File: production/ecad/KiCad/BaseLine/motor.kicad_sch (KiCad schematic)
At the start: 2 parts, among them M1 Motor_DC, U2 DRV8830DGQR

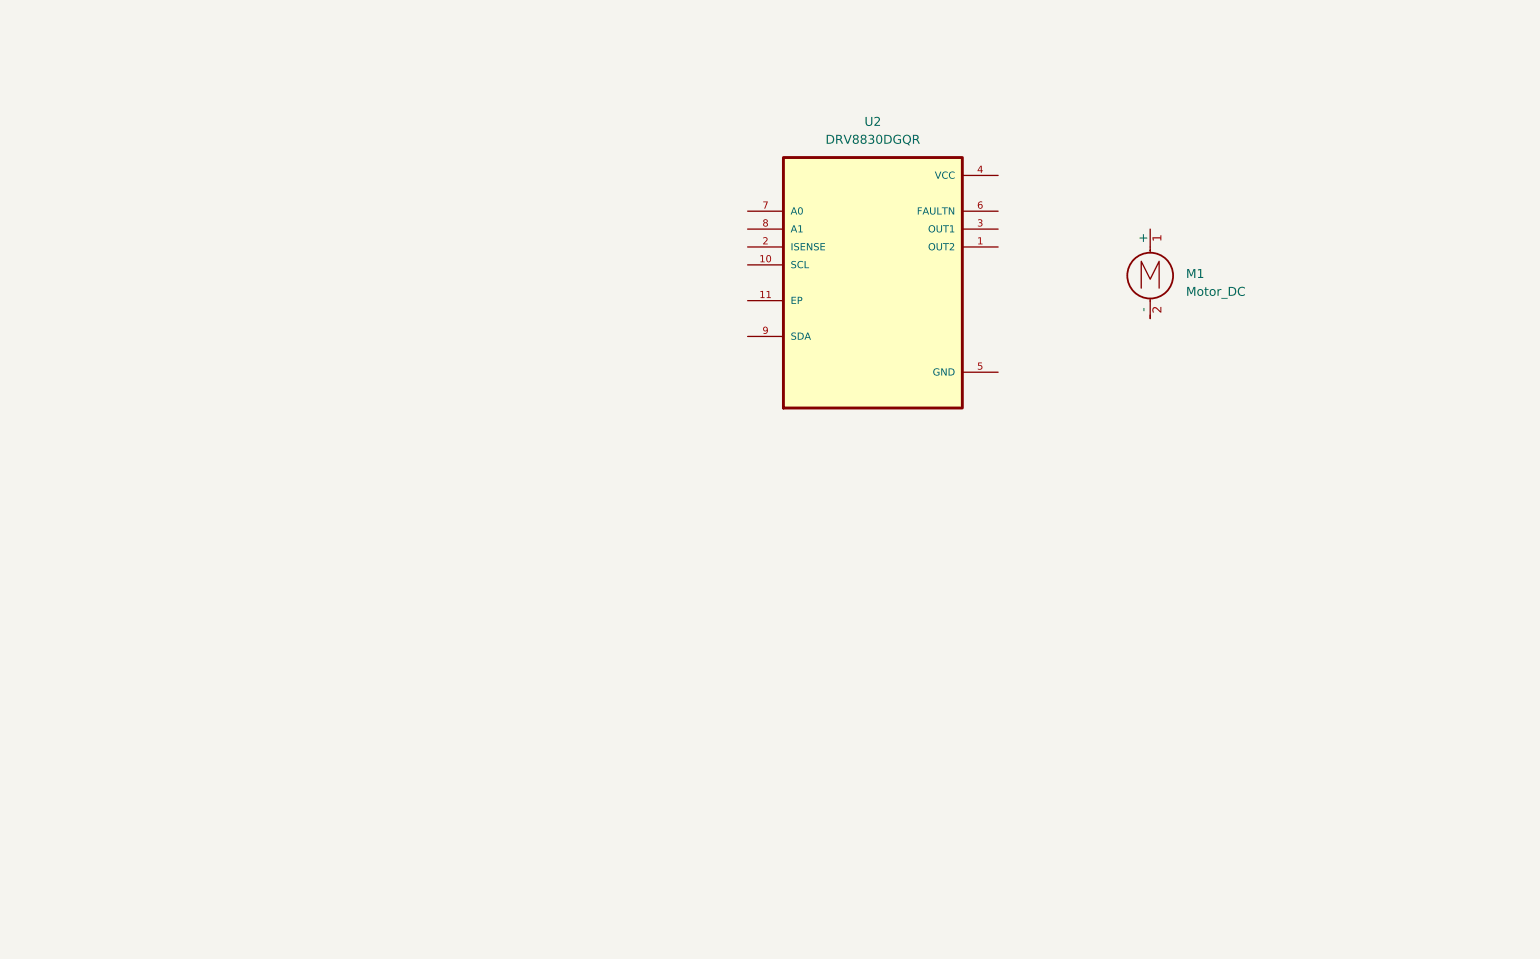
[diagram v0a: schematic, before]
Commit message: Added schematic for vibe motor
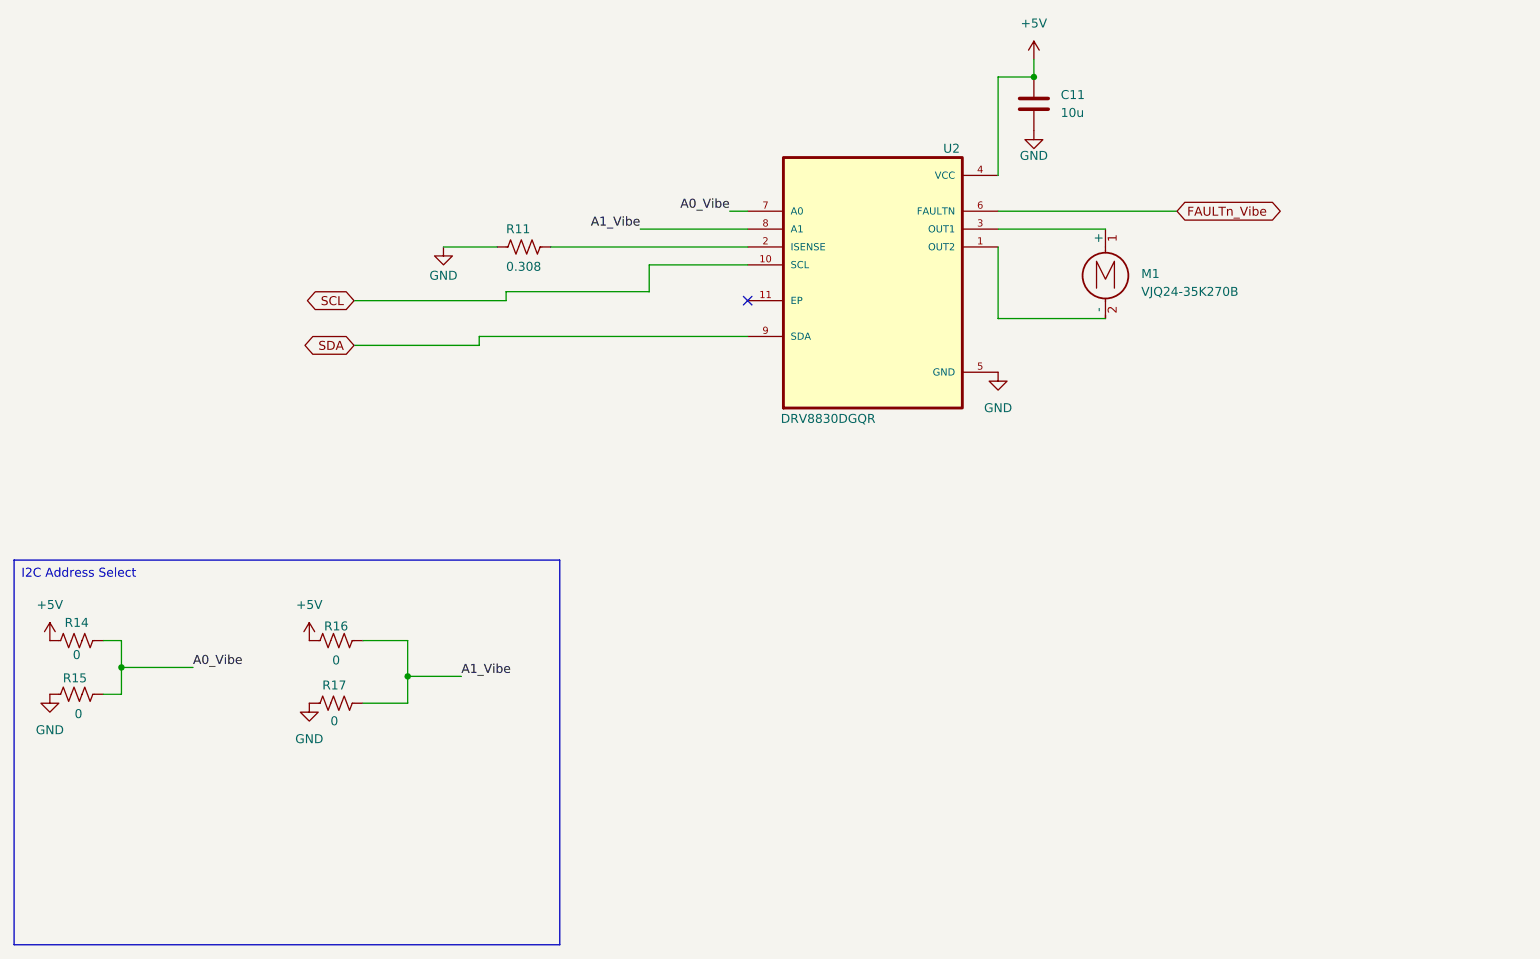
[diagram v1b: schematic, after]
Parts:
- added C11: 10u, symbol Device:C
- added R11: 0.308, symbol Device:R_US
- added R14, R15, R16, R17: 0, symbol Device:R_US
- M1: value Motor_DC -> VJQ24-35K270B
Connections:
- net at U2.1 (OUT2): now also M1.2 (-)
- net SCL: now reaches U2.10 (SCL)
- net at U2.2 (ISENSE): now also R11.1
- net at U2.3 (OUT1): now also M1.1 (+)
- net +5V: now reaches U2.4 (VCC)
- net +5V: now also C11.1, R14.1, R16.1
- net GND: now reaches U2.5 (GND)
- net GND: now also C11.2, R11.2, R15.1, R17.1
- net FAULTn_Vibe: now reaches U2.6 (FAULTN)
- net A0_Vibe: now reaches U2.7 (A0)
- net A0_Vibe: now also R14.2, R15.2
- net A1_Vibe: now reaches U2.8 (A1)
- net A1_Vibe: now also R16.2, R17.2
- net SDA: now reaches U2.9 (SDA)
- no-connect marks 0 -> 1
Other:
- moved on the sheet: M1

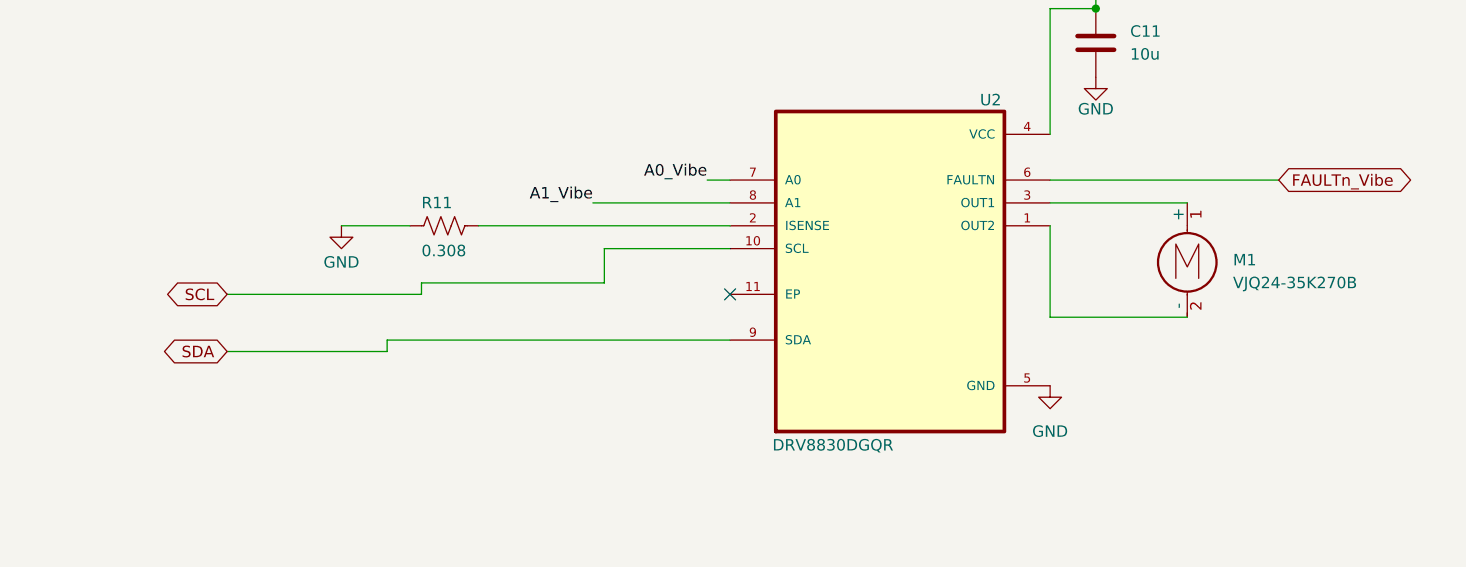
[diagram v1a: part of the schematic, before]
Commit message: Added vibe motor connector and amp I2C
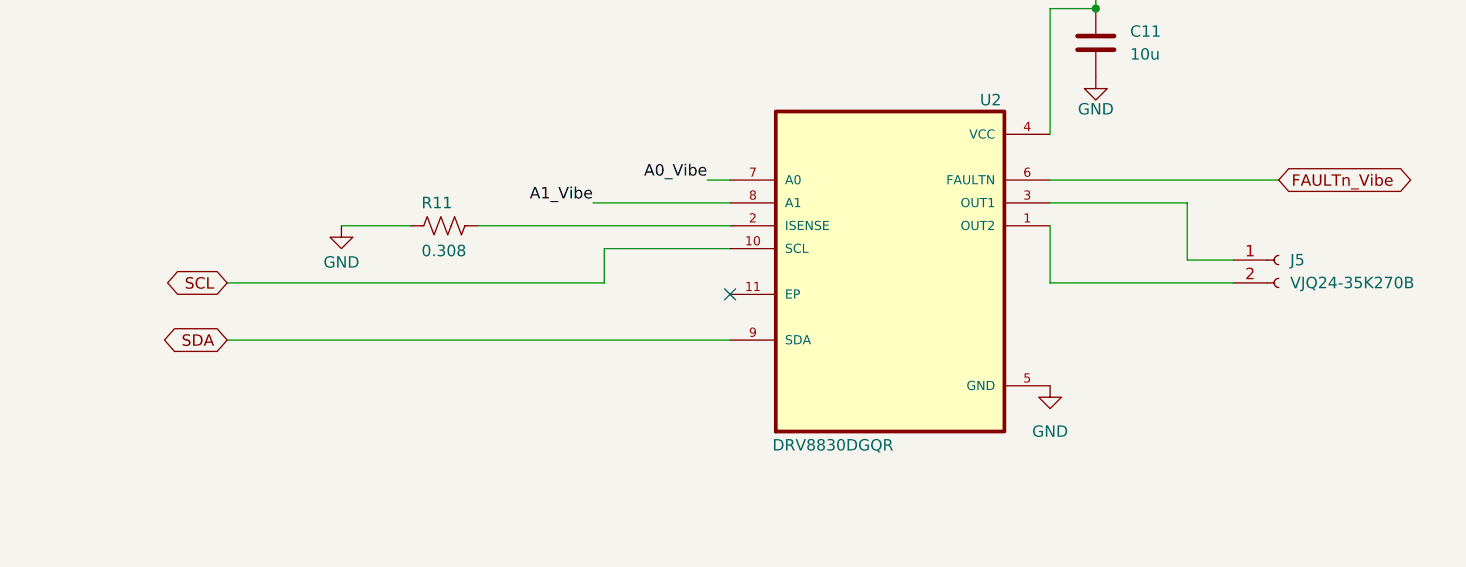
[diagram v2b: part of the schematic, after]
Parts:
- removed M1: VJQ24-35K270B, symbol Motor:Motor_DC
- added J5: VJQ24-35K270B, symbol Connector:Conn_01x02_Socket
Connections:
- net at U2.1 (OUT2): now also J5.2 (Pin_2)
- net at U2.3 (OUT1): now also J5.1 (Pin_1)
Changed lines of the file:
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@@
 	(wire
 		(pts
-			(xy 80.01 109.22) (xy 118.11 109.22)
+			(xy 168.91 100.33) (xy 173.99 100.33)
 		)
 		(stroke
@@
 	(wire
 		(pts
-			(xy 83.82 102.87) (xy 104.14 102.87)
+			(xy 153.67 102.87) (xy 153.67 96.52)
 		)
 		(stroke
@@
 	(wire
 		(pts
-			(xy 153.67 96.52) (xy 153.67 106.68)
+			(xy 29.21 152.4) (xy 26.67 152.4)
 		)
 		(stroke
@@
 	(wire
 		(pts
-			(xy 83.82 104.14) (xy 83.82 102.87)
+			(xy 153.67 72.39) (xy 153.67 86.36)
 		)
 		(stroke
@@
 	(wire
 		(pts
-			(xy 29.21 152.4) (xy 26.67 152.4)
+			(xy 168.91 93.98) (xy 168.91 100.33)
 		)
 		(stroke
@@
 	(wire
 		(pts
-			(xy 80.01 110.49) (xy 80.01 109.22)
+			(xy 153.67 72.39) (xy 158.75 72.39)
 		)
 		(stroke
@@
 	(wire
 		(pts
-			(xy 153.67 72.39) (xy 153.67 86.36)
+			(xy 90.17 96.52) (xy 118.11 96.52)
 		)
 		(stroke
@@
 	(wire
 		(pts
-			(xy 153.67 72.39) (xy 158.75 72.39)
+			(xy 104.14 99.06) (xy 118.11 99.06)
 		)
 		(stroke
@@
 	(wire
 		(pts
-			(xy 90.17 96.52) (xy 118.11 96.52)
+			(xy 63.5 152.4) (xy 69.85 152.4)
 		)
 		(stroke
@@
 	(wire
 		(pts
-			(xy 104.14 99.06) (xy 118.11 99.06)
+			(xy 62.23 102.87) (xy 104.14 102.87)
 		)
 		(stroke
@@
 	(wire
 		(pts
-			(xy 63.5 152.4) (xy 69.85 152.4)
+			(xy 115.57 91.44) (xy 118.11 91.44)
 		)
 		(stroke
@@
 	(wire
 		(pts
-			(xy 62.23 104.14) (xy 83.82 104.14)
+			(xy 29.21 160.02) (xy 29.21 156.21)
 		)
 		(stroke
@@
 	(wire
 		(pts
-			(xy 115.57 91.44) (xy 118.11 91.44)
+			(xy 153.67 91.44) (xy 179.07 91.44)
 		)
 		(stroke
@@
 	(wire
 		(pts
-			(xy 29.21 160.02) (xy 29.21 156.21)
+			(xy 39.37 156.21) (xy 29.21 156.21)
 		)
 		(stroke
@@
 	(wire
 		(pts
-			(xy 153.67 91.44) (xy 179.07 91.44)
+			(xy 62.23 109.22) (xy 118.11 109.22)
 		)
 		(stroke
@@
 	(wire
 		(pts
-			(xy 39.37 156.21) (xy 29.21 156.21)
+			(xy 69.85 157.48) (xy 77.47 157.48)
 		)
 		(stroke
@@
 	(wire
 		(pts
-			(xy 62.23 110.49) (xy 80.01 110.49)
+			(xy 69.85 157.48) (xy 69.85 161.29)
 		)
 		(stroke
@@
 	(wire
 		(pts
-			(xy 69.85 157.48) (xy 77.47 157.48)
-		)
-		(stroke
-			(width 0)
-			(type default)
-		)
-	)
-	(wire
-		(pts
-			(xy 153.67 106.68) (xy 168.91 106.68)
-		)
-		(stroke
-			(width 0)
-			(type default)
-		)
-	)
-	(wire
-		(pts
-			(xy 69.85 157.48) (xy 69.85 161.29)
+			(xy 153.67 102.87) (xy 173.99 102.87)
 		)
 		(stroke
@@
 	(global_label "SDA"
 		(shape bidirectional)
-		(at 62.23 110.49 180)
+		(at 62.23 109.22 180)
 		(fields_autoplaced yes)
 		(effects
@@
 		)
 		(property "Intersheetrefs" "${INTERSHEET_REFS}"
-			(at 54.5654 110.49 0)
+			(at 54.5654 109.22 0)
 			(effects
 				(font
@@
 	(global_label "SCL"
 		(shape bidirectional)
-		(at 62.23 104.14 180)
+		(at 62.23 102.87 180)
 		(fields_autoplaced yes)
 		(effects
@@
 		)
 		(property "Intersheetrefs" "${INTERSHEET_REFS}"
-			(at 54.6259 104.14 0)
+			(at 54.6259 102.87 0)
 			(effects
 				(font
@@
 	)
 	(symbol
+		(lib_id "Connector:Conn_01x02_Socket")
+		(at 179.07 100.33 0)
+		(unit 1)
+		(exclude_from_sim no)
+		(in_bom yes)
+		(on_board yes)
+		(dnp no)
+		(fields_autoplaced yes)
+		(property "Reference" "J5"
+			(at 180.34 100.3299 0)
+			(effects
+				(font
+					(size 1.27 1.27)
+				)
+				(justify left)
+			)
+		)
+		(property "Value" "VJQ24-35K270B"
+			(at 180.34 102.8699 0)
+			(effects
+				(font
+					(size 1.27 1.27)
+				)
+				(justify left)
+			)
+		)
+		(property "Footprint" ""
+			(at 179.07 100.33 0)
+			(effects
+				(font
+					(size 1.27 1.27)
+				)
+				(hide yes)
+			)
+		)
+		(property "Datasheet" "~"
+			(at 179.07 100.33 0)
+			(effects
+				(font
+					(size 1.27 1.27)
+				)
+				(hide yes)
+			)
+		)
+		(property "Description" "Generic connector, single row, 01x02, script generated"
+			(at 179.07 100.33 0)
+			(effects
+				(font
+					(size 1.27 1.27)
+				)
+				(hide yes)
+			)
+		)
+		(pin "2"
+		)
+		(pin "1"
+		)
+		(instances
+			(project "BaseLine"
+				(path "/ba9eda21-3882-41e1-8265-3d8ac781da20/32bcaf69-2ff4-46a9-8a42-fce7269397e2"
+					(reference "J5")
+					(unit 1)
+				)
+			)
+		)
+	)
+	(symbol
 		(lib_id "Device:C")
 		(at 158.75 76.2 0)
@@
 					(unit 1)
 				)
-			)
-		)
-	)
-	(symbol
-		(lib_id "Motor:Motor_DC")
-		(at 168.91 99.06 0)
-		(unit 1)
-		(exclude_from_sim no)
-		(in_bom yes)
-		(on_board yes)
-		(dnp no)
-		(fields_autoplaced yes)
-		(property "Reference" "M1"
-			(at 173.99 100.3299 0)
-			(effects
-				(font
-					(size 1.27 1.27)
-				)
-				(justify left)
-			)
-		)
-		(property "Value" "VJQ24-35K270B"
-			(at 173.99 102.8699 0)
-			(effects
-				(font
-					(size 1.27 1.27)
-				)
-				(justify left)
-			)
-		)
-		(property "Footprint" ""
-			(at 168.91 101.346 0)
-			(effects
-				(font
-					(size 1.27 1.27)
-				)
-				(hide yes)
-			)
-		)
-		(property "Datasheet" "https://www.digikey.com/en/products/detail/vybronics-inc/VJQ24-35K270B/7732324"
-			(at 168.91 101.346 0)
-			(effects
-				(font
-					(size 1.27 1.27)
-				)
-				(hide yes)
-			)
-		)
-		(property "Description" "DC Motor"
-			(at 168.91 99.06 0)
-			(effects
-				(font
-					(size 1.27 1.27)
-				)
-				(hide yes)
-			)
-		)
-		(pin "2"
-		)
-		(pin "1"
-		)
-		(instances
-			(project "BaseLine"
-				(path "/ba9eda21-3882-41e1-8265-3d8ac781da20/32bcaf69-2ff4-46a9-8a42-fce7269397e2"
-					(reference "M1")
-					(unit 1)
-				)

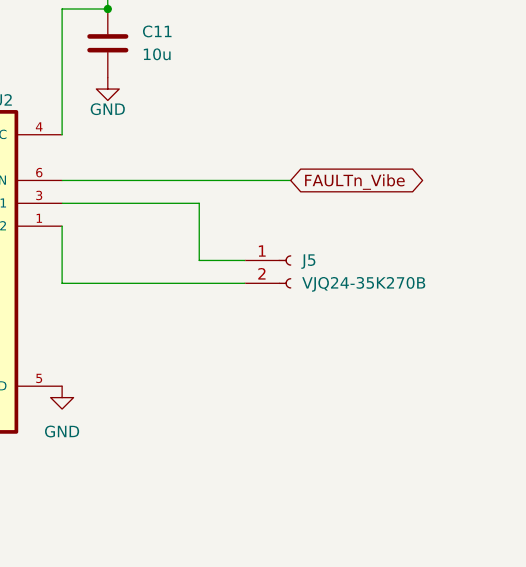
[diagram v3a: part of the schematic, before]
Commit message: Updated with new load cell amp IC
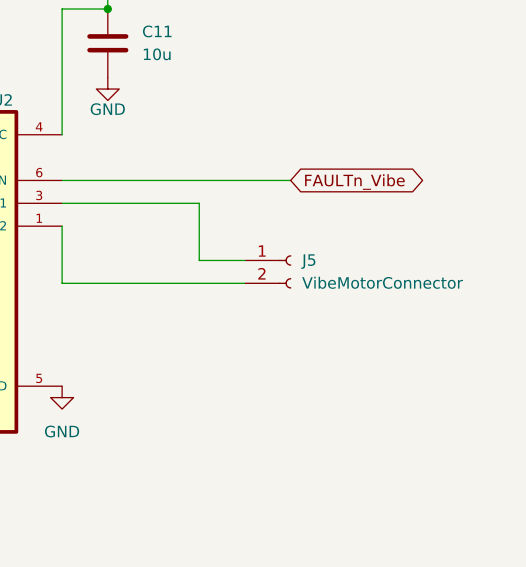
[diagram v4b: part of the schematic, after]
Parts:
- J5: value VJQ24-35K270B -> VibeMotorConnector
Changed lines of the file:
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@@
 			)
 		)
-		(property "Value" "VJQ24-35K270B"
+		(property "Value" "VibeMotorConnector"
 			(at 180.34 102.8699 0)
 			(effects
@@
 			)
 		)
-		(property "Datasheet" "~"
+		(property "Datasheet" "https://www.digikey.com/en/products/detail/vybronics-inc/VJQ24-35K270B/7732324?s=N4IgTCBcDaIGoCkCKYAsBaAzAVgNJgHYAGAIRAF0BfIA"
 			(at 179.07 100.33 0)
 			(effects
@@
 			)
 		)
-		(property "Description" "Generic connector, single row, 01x02, script generated"
+		(property "Description" "VJQ24-35K270B"
 			(at 179.07 100.33 0)
 			(effects

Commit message: Updates
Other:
- moved on the sheet: J5
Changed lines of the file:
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@@
 	(wire
 		(pts
-			(xy 168.91 100.33) (xy 173.99 100.33)
+			(xy 168.91 100.33) (xy 199.39 100.33)
 		)
 		(stroke
@@
 	(wire
 		(pts
-			(xy 153.67 102.87) (xy 173.99 102.87)
+			(xy 153.67 102.87) (xy 199.39 102.87)
 		)
 		(stroke
@@
 	(symbol
 		(lib_id "Connector:Conn_01x02_Socket")
-		(at 179.07 100.33 0)
+		(at 204.47 100.33 0)
 		(unit 1)
 		(exclude_from_sim no)
@@
 		(fields_autoplaced yes)
 		(property "Reference" "J5"
-			(at 180.34 100.3299 0)
+			(at 205.74 100.3299 0)
 			(effects
 				(font
@@
 		)
 		(property "Value" "VibeMotorConnector"
-			(at 180.34 102.8699 0)
+			(at 205.74 102.8699 0)
 			(effects
 				(font
@@
 		)
 		(property "Footprint" ""
-			(at 179.07 100.33 0)
+			(at 204.47 100.33 0)
 			(effects
 				(font
@@
 		)
 		(property "Datasheet" "https://www.digikey.com/en/products/detail/vybronics-inc/VJQ24-35K270B/7732324?s=N4IgTCBcDaIGoCkCKYAsBaAzAVgNJgHYAGAIRAF0BfIA"
-			(at 179.07 100.33 0)
+			(at 204.47 100.33 0)
 			(effects
 				(font
@@
 		)
 		(property "Description" "VJQ24-35K270B"
-			(at 179.07 100.33 0)
-			(effects
-				(font
+			(at 204.47 100.33 0)
+			(effects
+				(font
